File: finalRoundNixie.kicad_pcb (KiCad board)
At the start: 2 copper layers, 37 x 56.3 mm, 67 parts, among them J1 Conn_01x06_Male, J2 HV_IN, J3 Conn_01x06_Female, J4 HV_OUT, Q1 MMBTA42LT1, Q10 MMBTA42LT1, Q11 AO3400, Q12 AO3400, Q13 AO3400, Q14 MMBTA42LT1, Q15 MMBTA42LT1, Q2 MMBTA42LT1, Q3 MMBTA42LT1, Q4 MMBTA42LT1, Q5 MMBTA42LT1, Q6 MMBTA42LT1, Q7 MMBTA42LT1, Q8 MMBTA42LT1, Q9 MMBTA42LT1, U1 74HC595D, U2 nixie-tube, U3 74HC595D, U4 ams1117-5.0

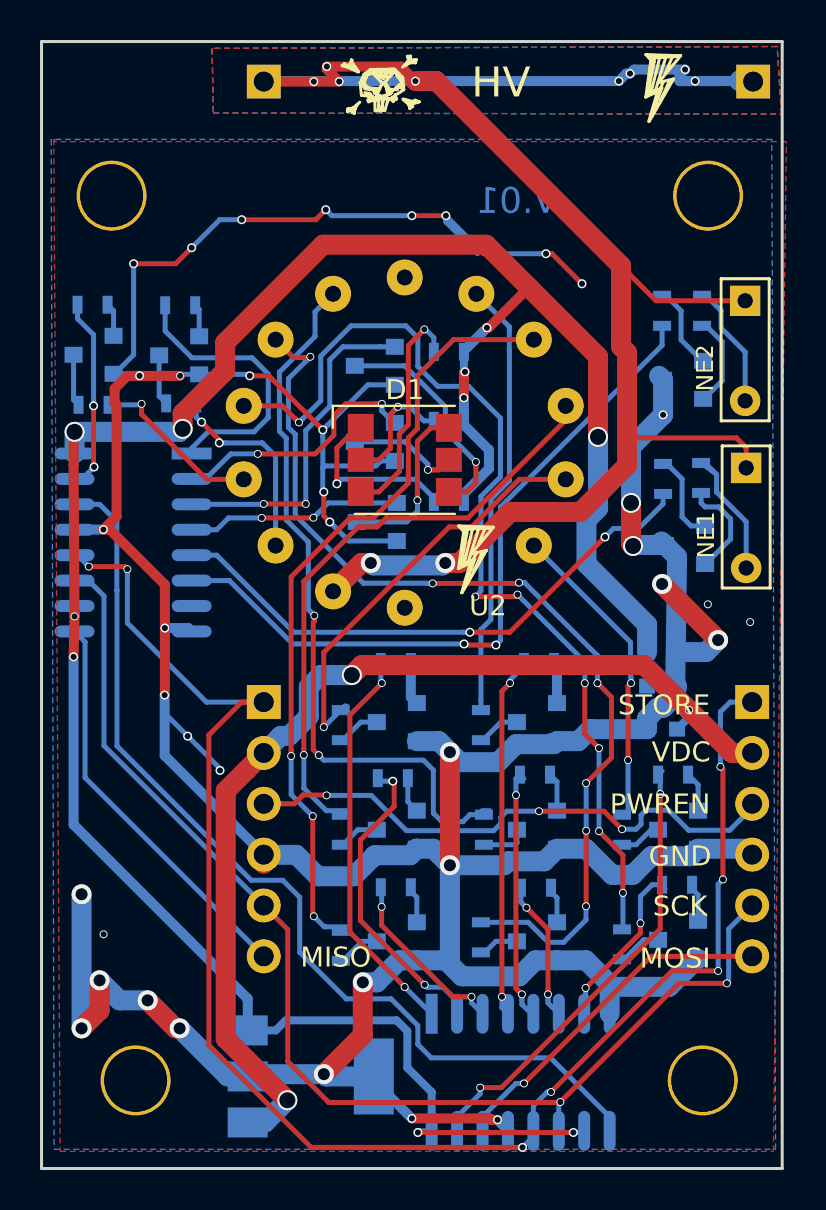
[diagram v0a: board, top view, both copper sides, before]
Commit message: fixed 2 of the mmbta42 transistor pin number errors
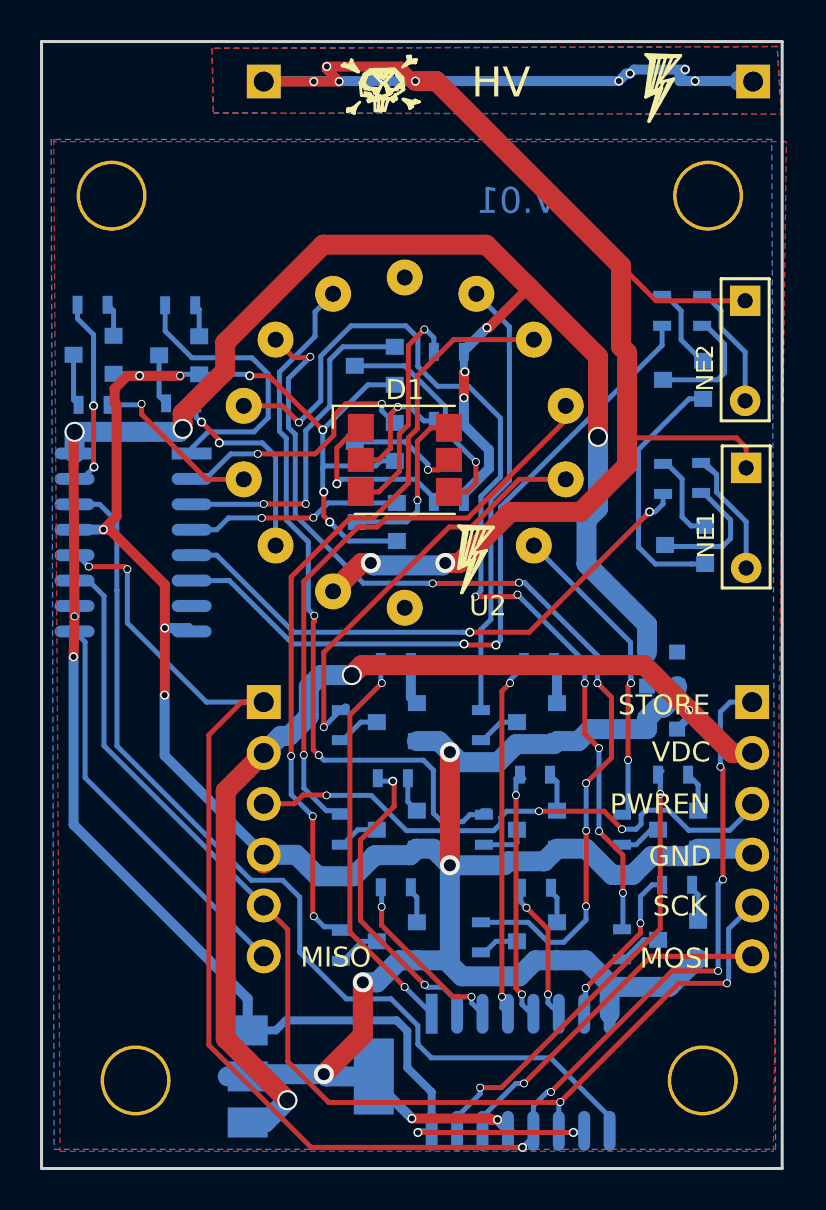
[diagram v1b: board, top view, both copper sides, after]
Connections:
- Q14 pad 2: Net-(Q14-Pad2) -> GND
- Q14 pad 3: GND -> Net-(Q14-Pad3)
- Q15 pad 2: Net-(Q15-Pad2) -> GND
- Q15 pad 3: GND -> Net-(Q15-Pad3)
- R25 pad 2: Net-(Q14-Pad2) -> Net-(Q14-Pad3)
- R27 pad 2: Net-(Q15-Pad2) -> Net-(Q15-Pad3)
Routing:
- net GND: track 238.9 -> 170.3 mm, vias 35 -> 15
- net Net-(Q14-Pad3): track 0.00 -> 6.43 mm
- net Net-(Q15-Pad3): track 0.00 -> 6.15 mm
- net Net-(Q14-Pad2): track 5.10 -> 0.00 mm
- net Net-(Q15-Pad2): track 4.60 -> 0.00 mm
- net (no net): vias 3 -> 0

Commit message: fixed ams1117 pin numbering errors
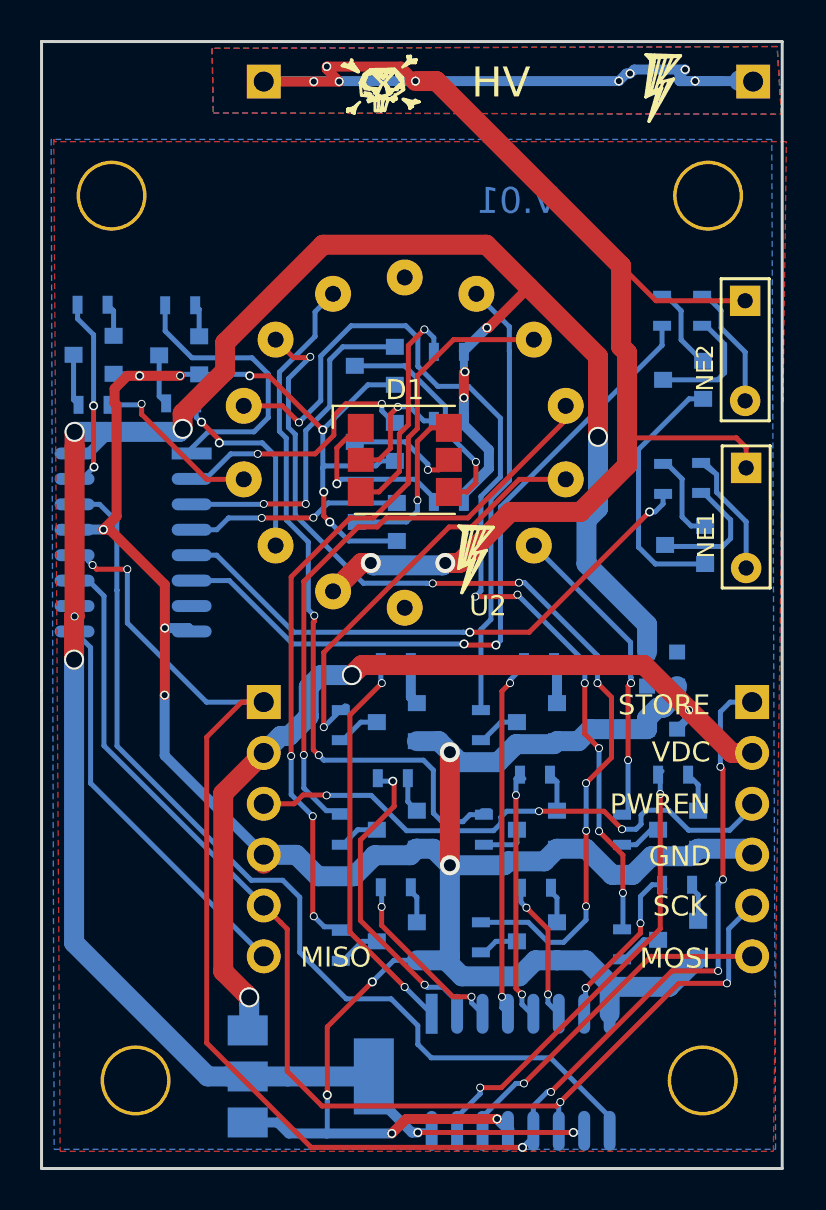
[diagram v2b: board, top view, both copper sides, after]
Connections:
- U4 pad 1: +VDC -> GND
- U4 pad 2: GND -> +5V
- U4 pad 3: +5V -> +VDC
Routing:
- net +VDC: track 52.3 -> 45.4 mm
- net +5V: track 123.1 -> 125.2 mm
- net GND: track 170.3 -> 171.8 mm

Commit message: nixie's legs pin assignment needs to be change
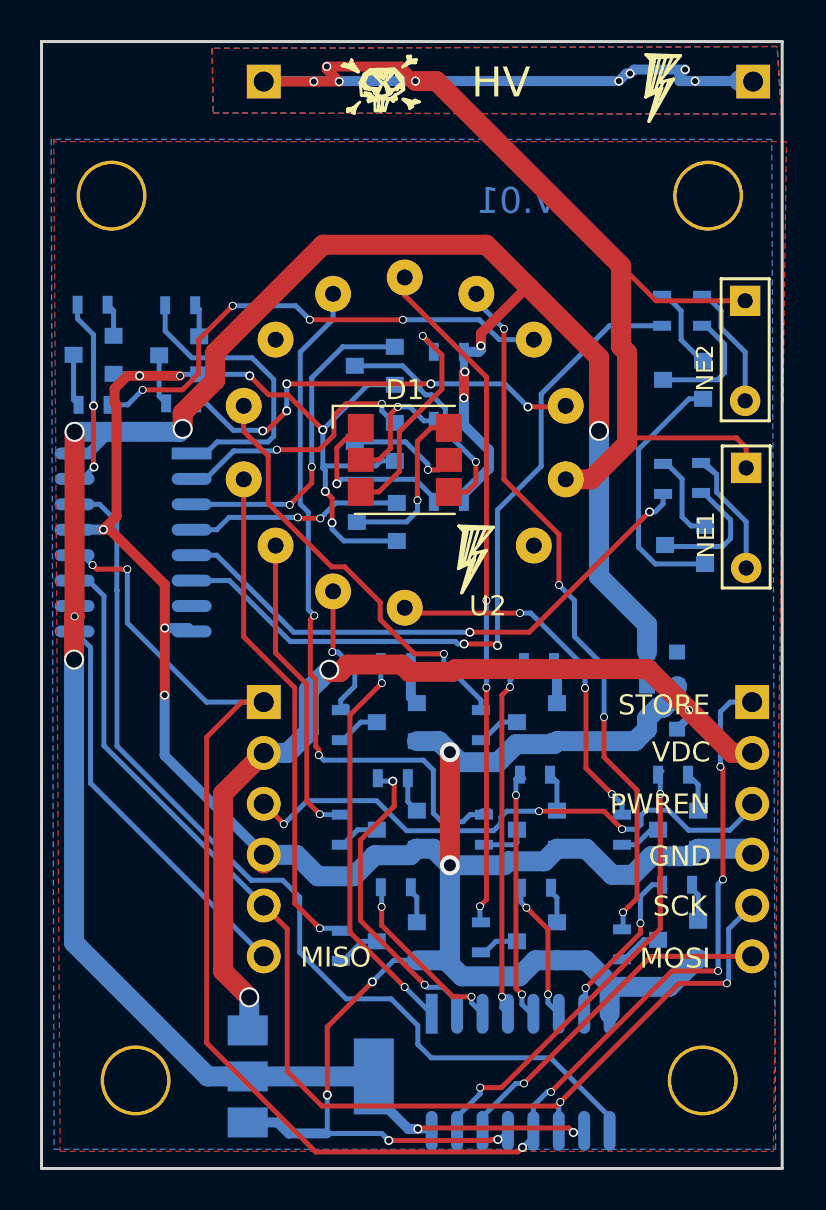
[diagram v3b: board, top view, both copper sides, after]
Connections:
- R14 pad 2: /s9 -> /s0
- R15 pad 1: /s4 -> /s5
- R16 pad 1: /s8 -> /s1
- R17 pad 1: /s3 -> /s6
- R18 pad 1: /s2 -> /s7
- R19 pad 1: /s7 -> /s2
- R20 pad 1: /s1 -> /s8
- R21 pad 1: /s6 -> /s3
- R22 pad 1: /s0 -> /s9
- R23 pad 1: /s5 -> /s4
- U1 pad 1: /s1 -> /s8
- U1 pad 15: /s0 -> /s9
- U1 pad 2: /s2 -> /s7
- U1 pad 3: /s3 -> /s6
- U1 pad 4: /s4 -> /s5
- U1 pad 5: /s5 -> /s4
- U1 pad 6: /s6 -> /s3
- U1 pad 7: /s7 -> /s2
- U3 pad 1: /s9 -> /s0
- U3 pad 15: /s8 -> /s1
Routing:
- net Net-(R2-Pad1): track 8.64 -> 25.0 mm, vias 1 -> 4
- net Net-(R4-Pad1): track 48.8 -> 34.1 mm, vias 7 -> 3
- net Net-(R8-Pad1): track 30.1 -> 15.4 mm
- net Net-(J2-Pad1): track 92.4 -> 77.7 mm, vias 10 -> 8
- net Net-(R7-Pad1): track 39.2 -> 25.1 mm, vias 3 -> 1
- net Net-(R9-Pad1): track 21.0 -> 6.97 mm
- net Net-(R3-Pad1): track 49.7 -> 36.1 mm, vias 7 -> 4
- net Net-(R1-Pad1): track 10.2 -> 22.2 mm, vias 2 -> 5
- net /s8: track 10.2 -> 19.9 mm
- net /s1: track 19.9 -> 10.2 mm
- net /s9: track 14.2 -> 22.8 mm, vias 0 -> 2
- net /s0: track 22.8 -> 15.0 mm, vias 2 -> 0
- net /s7: track 8.38 -> 15.7 mm
- net /s2: track 15.7 -> 8.38 mm
- net /s5: track 12.6 -> 18.2 mm
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
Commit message: straighten some tracks
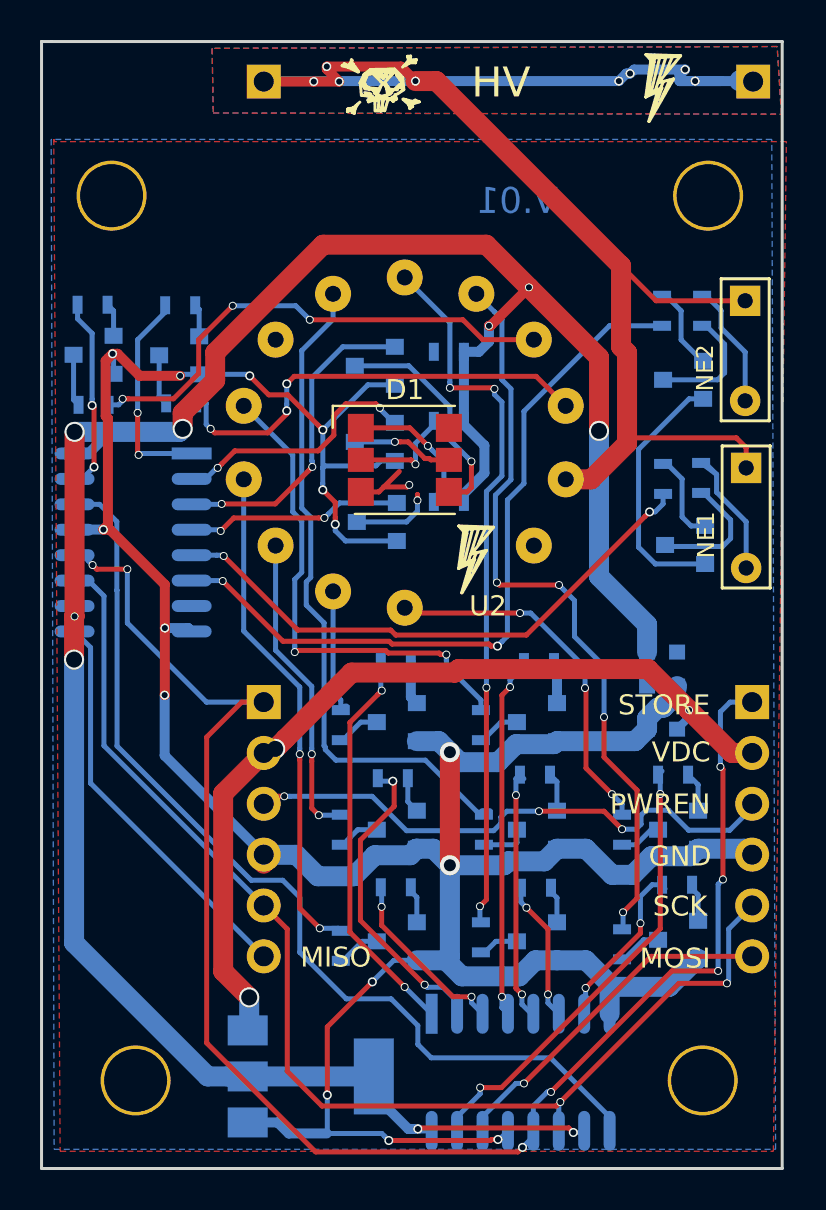
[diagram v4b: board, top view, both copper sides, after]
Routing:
- net Net-(D1-Pad3): track 11.7 -> 4.10 mm
- net Net-(D1-Pad6): track 8.64 -> 4.13 mm
- net /s0: track 15.0 -> 11.4 mm, vias 0 -> 2
- net Net-(R6-Pad1): track 21.4 -> 24.8 mm, vias 1 -> 2
- net Net-(R3-Pad1): track 36.1 -> 38.5 mm
- net Net-(R5-Pad1): track 35.7 -> 33.8 mm, vias 2 -> 0
- net Net-(R4-Pad1): track 34.1 -> 36.0 mm, vias 3 -> 4
- net Net-(D1-Pad1): track 9.13 -> 7.46 mm
- net +VDC: track 46.0 -> 44.4 mm
- net GND: track 171.7 -> 173.2 mm
- net Net-(R1-Pad1): track 22.2 -> 23.3 mm, vias 5 -> 3
- net Net-(R9-Pad1): track 6.97 -> 6.19 mm, vias 1 -> 0
- net /PWREN: track 28.5 -> 27.8 mm
- net Net-(D1-Pad5): track 5.89 -> 5.31 mm
- net +5V: track 125.2 -> 125.6 mm, vias 10 -> 9
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
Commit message: routed all tracks to fixed pin numbering on nixie tubes
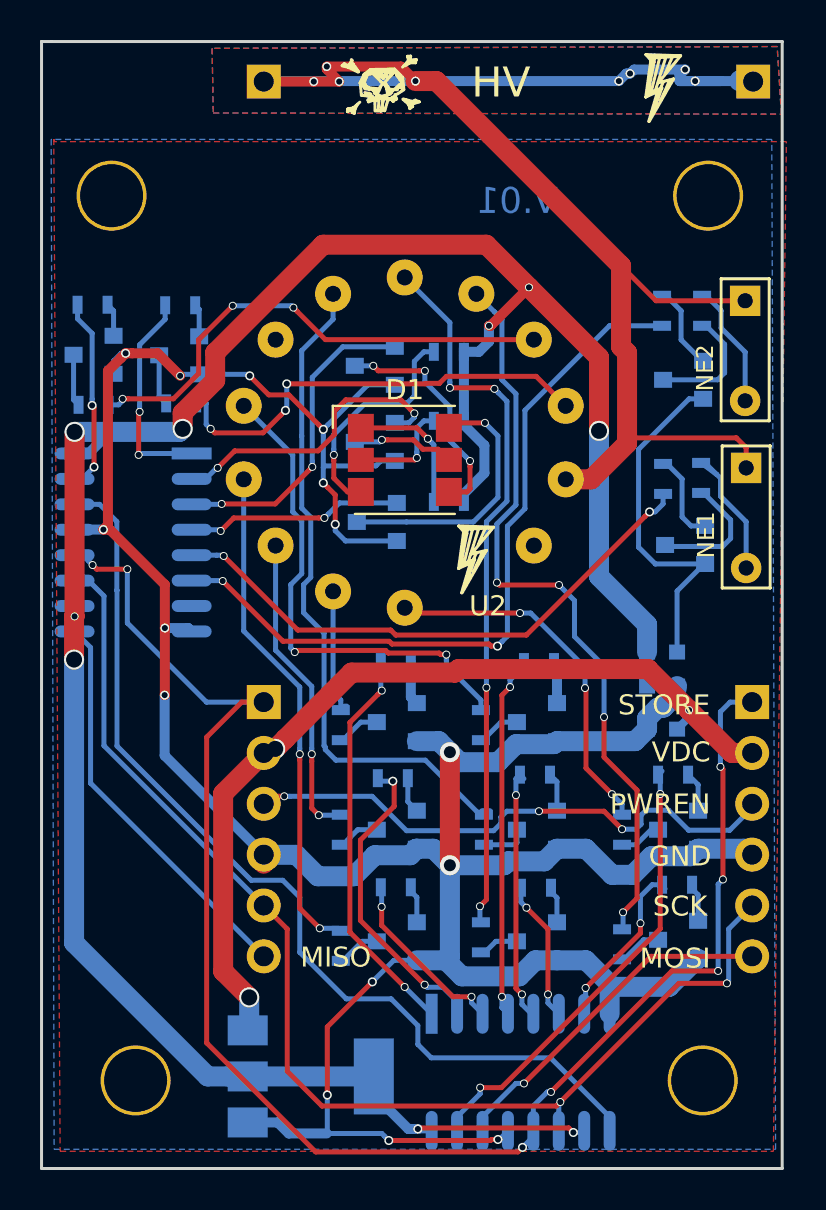
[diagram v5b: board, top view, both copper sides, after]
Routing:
- net Net-(D1-Pad6): track 4.13 -> 13.5 mm
- net Net-(D1-Pad3): track 4.10 -> 11.8 mm
- net GND: track 173.2 -> 178.2 mm
- net /Red: track 12.7 -> 15.1 mm
- net Net-(D1-Pad4): track 11.6 -> 11.8 mm, vias 1 -> 3
